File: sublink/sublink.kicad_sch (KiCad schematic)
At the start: 45 parts, among them J1 ZL315-4SGH, Q1 Q_PMOS_GSD, SW1 SW_Push, SW2 SW_Push, SW3 SW_Push, U1 ATtiny414-SS, U2 OKY3402, U3 JS202011

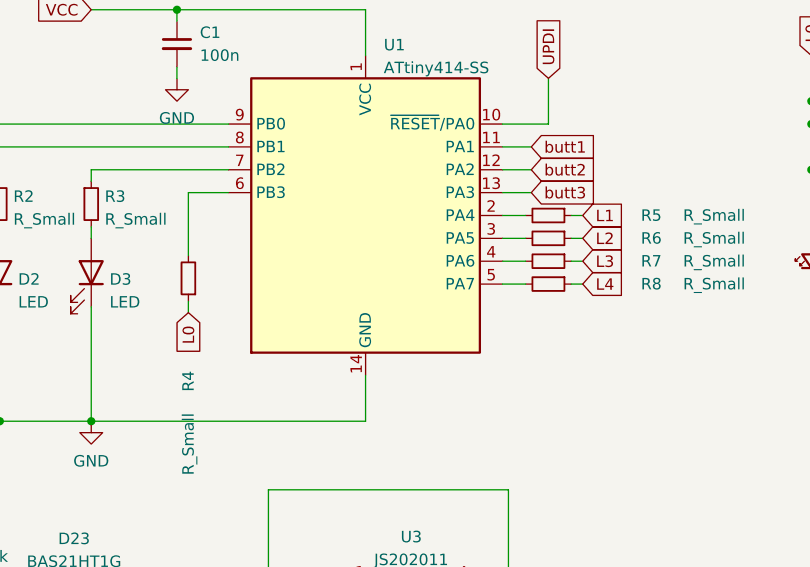
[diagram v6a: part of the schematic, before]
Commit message: bottom circle routing. Broke chargin part footprint for some reason
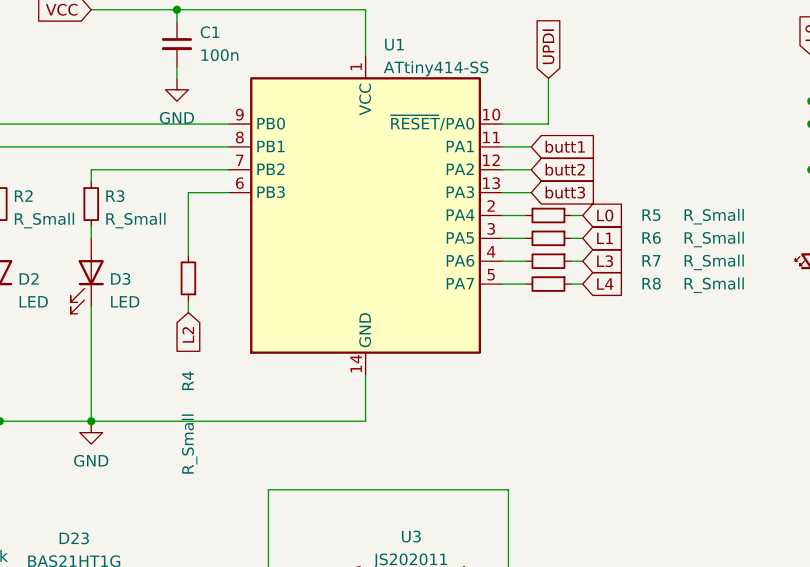
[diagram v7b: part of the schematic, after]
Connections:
- net L0: now also R5.1; no longer R4.1
- net L1: now also R6.1; no longer R5.1
- net L2: now also R4.1; no longer R6.1
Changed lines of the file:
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@@
     )
   )
-  (global_label "L0" (shape input) (at 107.315 62.865 270) (fields_autoplaced)
+  (global_label "L2" (shape input) (at 107.315 62.865 270) (fields_autoplaced)
     (effects (font (size 1.27 1.27)) (justify right))
-    (property "Intersheet References" "${INTERSHEET_REFS}" (id 0) (at 107.3944 67.5157 90)
+    (property "Intersheet References" "${INTERSHEET_REFS}" (id 0) (at 107.2356 67.5157 90)
       (effects (font (size 1.27 1.27)) (justify right) hide)
     )
@@
     )
   )
-  (global_label "L2" (shape input) (at 151.13 54.61 0) (fields_autoplaced)
+  (global_label "L1" (shape input) (at 151.13 54.61 0) (fields_autoplaced)
     (effects (font (size 1.27 1.27)) (justify left))
     (property "Intersheet References" "${INTERSHEET_REFS}" (id 0) (at 155.7807 54.5306 0)
@@
     )
   )
-  (global_label "L1" (shape input) (at 151.13 52.07 0) (fields_autoplaced)
+  (global_label "L0" (shape input) (at 151.13 52.07 0) (fields_autoplaced)
     (effects (font (size 1.27 1.27)) (justify left))
     (property "Intersheet References" "${INTERSHEET_REFS}" (id 0) (at 155.7807 51.9906 0)
